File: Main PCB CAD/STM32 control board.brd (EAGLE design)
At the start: 120 x 100 mm, 193 parts, among them J10 B6B-PH, J15 DG301-4P, J16 B10B-PH, J17 B10B-PH, J18 B10B-PH, J19 B10B-PH, J20 B3B-PH, J21 B3B-PH, J22 B3B-PH, J23 B3B-PH, J4 PC_1733570, J5 PC_1733570, J6 B3B-PH, J7 B3B-PH, J8 B4B-PH, J9 B6B-PH, SW1 B3F-4055, SW2 B3F-4055, SW3 B3F-4055, SW4 B3F-4055, SW5 B3F-4055, U1 STM32G474, U2 TPS7A19, U3 REF3330, U4 REF3318, U5 ICM_20600, U6 DRV8701VIA, U8 L2293Q, X1 CSTNE

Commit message: Not finished consept
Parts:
- removed D2, D3, D4, D5: Blue, Semiconductor_devices:LED-0805
- removed RM1: RES_ARRAY0603, Resistors:0603-ARC
- moved J4 28.0 mm to (98.5, 117.0)
- moved J5 28.0 mm to (88.5, 117.0)
- moved RM5 18.8 mm to (105.4, 60.2), turned to 0 degrees
- moved RM3 18.0 mm to (82.4, 60.0), turned to 0 degrees
- moved J15 15.3 mm to (94.8, 89.8)
- moved D14 7.99 mm to (82.5, 46.2), turned to 0 degrees
- moved D15 7.99 mm to (82.5, 48.2), turned to 0 degrees
- moved D24 7.99 mm to (82.5, 50.2), turned to 0 degrees
- moved D25 7.99 mm to (82.5, 52.2), turned to 0 degrees
- moved D26 7.99 mm to (82.5, 54.2), turned to 0 degrees
- moved D35 7.99 mm to (82.5, 42.2), turned to 0 degrees
- moved D36 7.99 mm to (82.5, 44.2), turned to 0 degrees
- moved D37 7.99 mm to (82.5, 56.2), turned to 0 degrees
- moved J16 7.29 mm to (86.8, 49.2)
- moved RM2 5.70 mm to (82.4, 38.5)
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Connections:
- removed net N$13: D31.-, RM5.1
- removed net N$14: D32.-, RM5.2
- removed net N$17: D33.-, RM5.3
- removed net N$22: D34.-, RM5.4
- removed net PB1: D4.+, U1.33
- removed net PB2: D5.+, U1.34
- removed net PC6: D2.+, U1.65
- removed net PC7: D3.+, U1.66
- net GND: no longer RM1.5, RM1.6, RM1.7, RM1.8
- net N$10: now also D34.-, RM5.1; no longer D30.-, RM4.4
- net N$11: now also D28.-, RM4.3; no longer D5.-, RM1.4
- net N$12: now also RM4.4; no longer RM4.1
- net N$3: now also D30.-, RM4.1; no longer D28.-, RM4.2
- net N$4: now also D31.-, RM5.4; no longer D2.-, RM1.1
- net N$5: now also D32.-, RM5.3; no longer D3.-, RM1.2
- net N$6: now also D33.-, RM5.2; no longer D4.-, RM1.3
- net N$9: now also RM4.2; no longer RM4.3
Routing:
- net GND: track 59.2 -> 35.8 mm
- net PD0: track 64.4 -> 41.8 mm
- net N$22: track 20.8 -> 0.00 mm, vias 2 -> 0
- net PD1: track 63.5 -> 43.0 mm
- net PD2: track 63.1 -> 44.3 mm
- net N$17: track 18.4 -> 0.00 mm, vias 2 -> 0
- net PD3: track 62.1 -> 45.5 mm
- net N$14: track 16.1 -> 0.00 mm, vias 2 -> 0
- net N$31: track 20.8 -> 4.99 mm
- net PD4: track 62.3 -> 46.8 mm
- net PD5: track 62.5 -> 48.0 mm
- net N$13: track 13.8 -> 0.00 mm, vias 2 -> 0
- net PD6: track 62.8 -> 49.2 mm
- net PD8: track 29.6 -> 16.5 mm
- net PD7: track 63.0 -> 50.5 mm
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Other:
- outline, holes or cut-outs redrawn

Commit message: consept update
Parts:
- moved D27 3.29 mm to (108.8, 43.0), turned to 0 degrees
- moved D28 3.29 mm to (108.8, 45.0), turned to 0 degrees
- moved D29 3.29 mm to (108.8, 47.0), turned to 0 degrees
- moved D30 3.29 mm to (108.8, 49.0), turned to 0 degrees
- moved D31 3.29 mm to (108.8, 51.0), turned to 0 degrees
- moved D32 3.29 mm to (108.8, 53.0), turned to 0 degrees
- moved D33 3.29 mm to (108.8, 55.0), turned to 0 degrees
- moved D34 3.29 mm to (108.8, 57.0), turned to 0 degrees
- moved J19 3.29 mm to (113.0, 50.0)
- moved RM4 3.29 mm to (108.9, 39.3)
- moved RM5 3.29 mm to (108.6, 60.7)
- moved D14 0.75 mm to (82.5, 47.0)
- moved D15 0.75 mm to (82.5, 49.0)
- moved D24 0.75 mm to (82.5, 51.0)
- moved D25 0.75 mm to (82.5, 53.0)
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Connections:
- net N$10: now also D28.-, RM4.2; no longer D34.-, RM5.1
- net N$11: now also D29.-; no longer D28.-
- net N$12: now also D30.-; no longer D27.-
- net N$3: now also D34.-, RM5.4; no longer D30.-, RM4.1
- net N$4: now also D33.-, RM5.3; no longer D31.-, RM5.4
- net N$5: now also RM5.2; no longer RM5.3
- net N$6: now also D31.-, RM5.1; no longer D33.-, RM5.2
- net N$9: now also D27.-, RM4.1; no longer D29.-, RM4.2
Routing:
- net PD0: track 41.8 -> 69.2 mm
- net PD1: track 43.0 -> 68.6 mm
- net PD2: track 44.3 -> 68.1 mm
- net PD3: track 45.5 -> 67.5 mm
- net PD4: track 46.8 -> 67.0 mm
- net PD5: track 48.0 -> 66.4 mm
- net PD6: track 49.2 -> 65.9 mm
- net PD7: track 50.5 -> 65.3 mm
- net N$12: track 4.61 -> 12.1 mm
- net N$3: track 11.9 -> 4.96 mm
- net N$6: track 6.85 -> 12.2 mm
- net N$4: track 11.8 -> 7.29 mm
- net N$9: track 9.33 -> 4.87 mm
- net N$10: track 4.52 -> 7.20 mm
- net N$11: track 6.94 -> 9.60 mm
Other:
- outline, holes or cut-outs redrawn

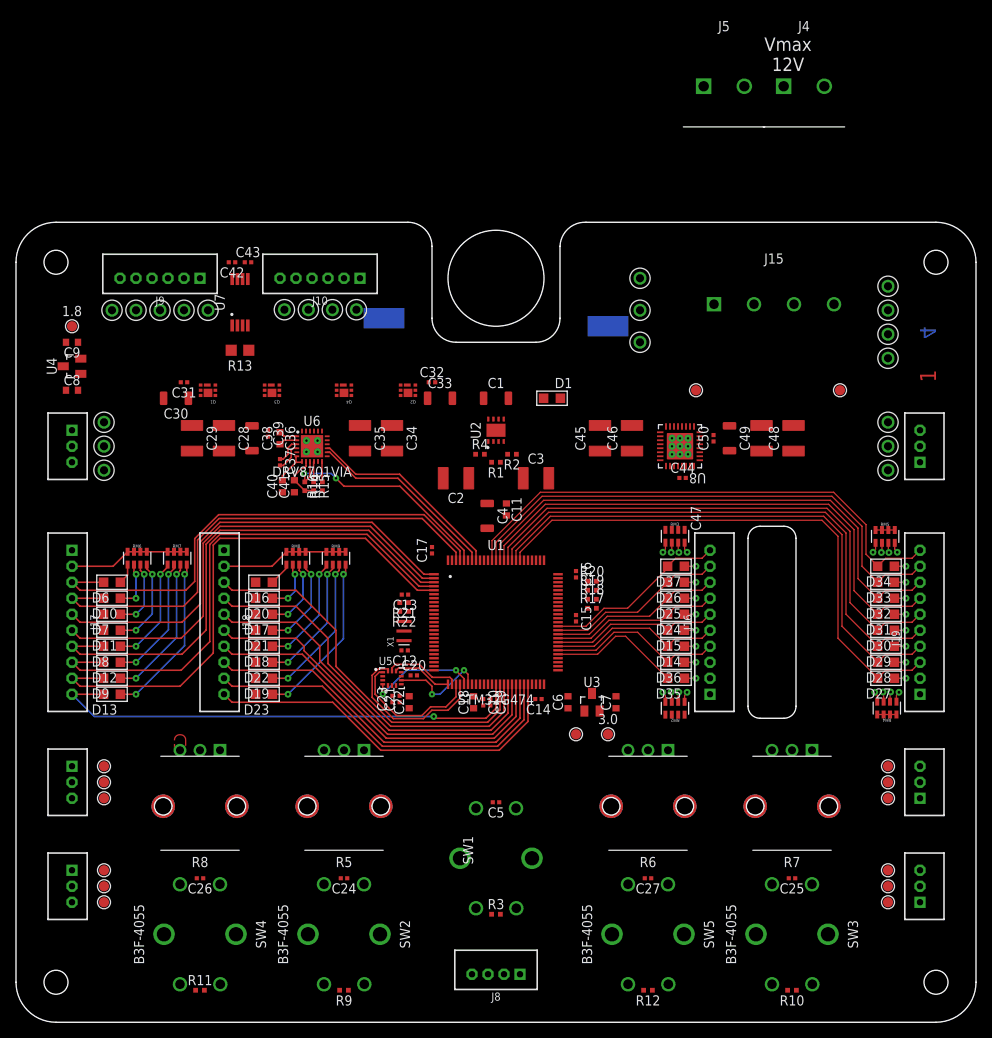
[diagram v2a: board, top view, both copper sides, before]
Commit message: placement fixes.
Current size is 104*120mm
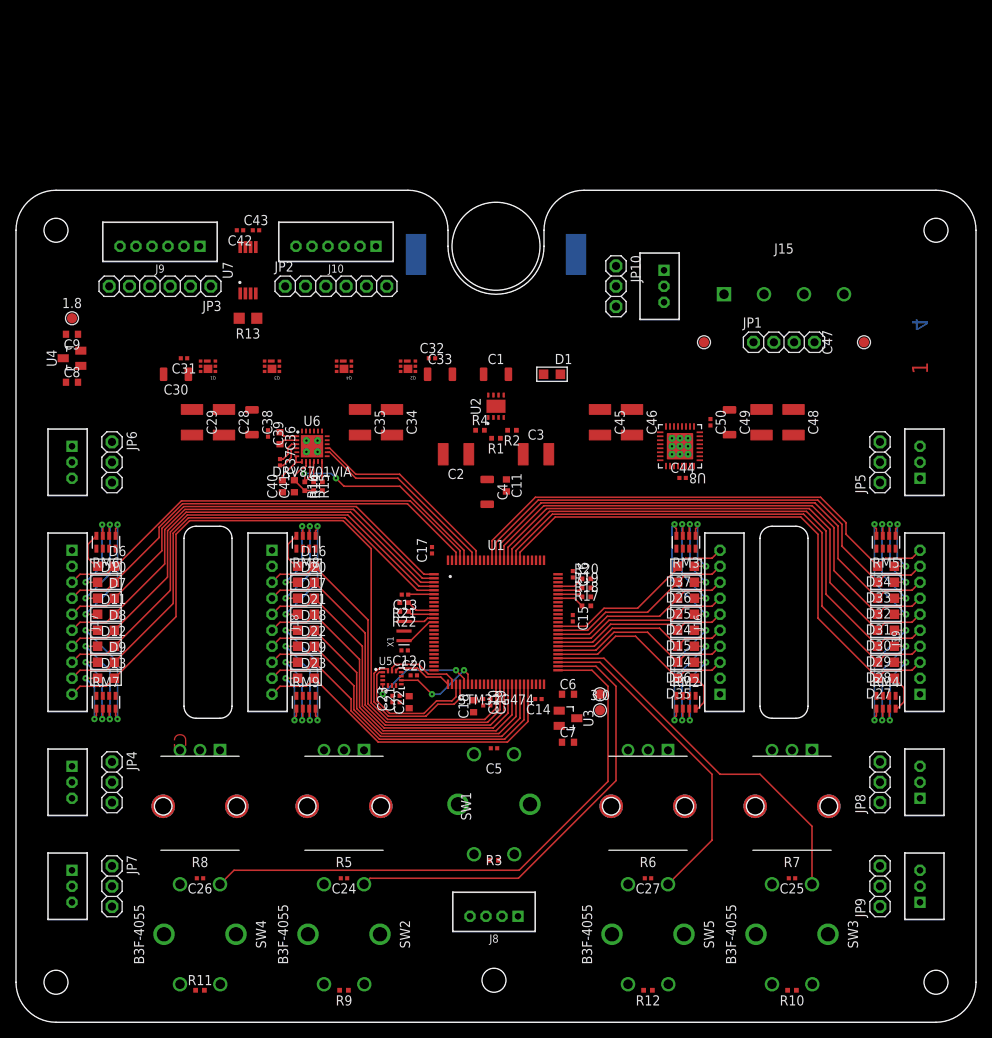
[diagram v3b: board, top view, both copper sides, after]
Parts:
- removed J4, J5: PC_1733570, Terminal blocks:PC_1733570
- removed TP1, TP18, TP19, TP2, TP20, TP21, TP22, TP23, TP24, TP25, TP26, TP27, TP28, TP29, TP3, TP30, TP31, TP32, TP33, TP34, TP35, TP36: (no value), testing:TEST_RING
- removed TP10, TP11, TP12, TP13, TP14, TP15, TP16, TP17, TP6, TP7, TP8, TP9: (no value), testing:TP1.27MM_MASK_SILKSCREEN
- added J1: B3B-PH, con-jst-ph:B3B-PH-K
- added JP1: (no value), commonly used connectors:1X04
- added JP10, JP4, JP5, JP6, JP7, JP8, JP9: (no value), commonly used connectors:1X03
- added JP2, JP3: (no value), commonly used connectors:1X06
- moved RM7 20.1 mm to (11.2, 40.0), turned to 180 degrees
- moved RM9 18.4 mm to (36.2, 40.0), turned to 180 degrees
- moved POS 9.85 mm to (70.0, 96.0), turned to 180 degrees
- moved NEG 8.94 mm to (50.0, 96.0), turned to 180 degrees
- moved C7 7.81 mm to (69.0, 35.0), turned to 0 degrees
- moved J8 7.25 mm to (59.8, 13.2)
- moved C5 6.75 mm to (59.8, 34.2)
- moved R3 6.75 mm to (59.8, 20.2)
- moved SW1 6.75 mm to (59.8, 27.2)
- moved TP38 6.71 mm to (106.0, 85.0)
- moved TP37 6.08 mm to (86.0, 85.0)
- moved J18 6.00 mm to (32.0, 50.0)
- moved GND_ 5.83 mm to (73.0, 41.0)
- moved D16 5.62 mm to (36.2, 57.0), turned to 180 degrees
- moved D17 5.62 mm to (36.2, 53.0), turned to 180 degrees
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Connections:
- removed net PC13: C26.1, R11.1, SW4.1, SW4.2, U1.7
- removed net PC14: C27.1, R12.1, SW5.1, SW5.2, U1.8
- new net PB12: C26.1, R11.1, SW4.1, SW4.2, U1.51
- new net PB13: C24.1, R9.1, SW2.1, SW2.2, U1.52
- net +3V: now also JP4.1, JP7.1, JP8.1, JP9.1; no longer TP12.1, TP15.1, TP6.1, TP9.1
- net +3V3: now also J1.2, JP10.2, JP2.2, JP3.1; no longer TP1.1
- net ENCODER_1: now also JP2.3; no longer TP30.1
- net ENCODER_2: now also JP2.4; no longer TP29.1
- net GND: now also J1.3, JP10.3, JP2.5, JP3.6, JP4.3, JP5.3, JP6.3, JP7.3, JP8.3, JP9.3, RM2.1, RM2.2, RM2.3, RM2.4, RM3.1, RM3.2, RM3.3, RM3.4, RM4.1, RM4.2, RM4.3, RM4.4, RM5.1, RM5.2, RM5.3, RM5.4, RM6.1, RM6.2, RM6.3, RM6.4, RM7.1, RM7.2, RM7.3, RM7.4, RM8.1, RM8.2, RM8.3, RM8.4, RM9.1, RM9.2, RM9.3, RM9.4; no longer RM2.5, RM2.6, RM2.7, RM2.8, RM3.5, RM3.6, RM3.7, RM3.8, RM4.5, RM4.6, RM4.7, RM4.8, RM5.5, RM5.6, RM5.7, RM5.8, RM6.5, RM6.6, RM6.7, RM6.8, RM7.5, RM7.6, RM7.7, RM7.8, RM8.5, RM8.6, RM8.7, RM8.8, RM9.5, RM9.6, RM9.7, RM9.8, TP11.1, TP14.1, TP17.1, TP20.1, TP21.1, TP26.1, TP3.1, TP32.1, TP8.1
- net I2C3_SCL: now also JP5.2; no longer TP27.1
- net I2C3_SDA: now also JP5.1; no longer TP28.1
- net M1: now also JP2.1; no longer TP31.1
- net M_SH2: now also JP2.6
- net N$10: now also RM4.7; no longer RM4.2
- net N$11: now also RM4.6; no longer RM4.3
- net N$12: now also RM4.5; no longer RM4.4
- net N$23: now also RM2.8; no longer RM2.1
- net N$25: now also RM2.7; no longer RM2.2
- net N$26: now also RM2.6; no longer RM2.3
- net N$27: now also RM2.5; no longer RM2.4
- net N$28: now also RM3.8; no longer RM3.1
- net N$29: now also RM3.7; no longer RM3.2
- net N$3: now also RM5.5; no longer RM5.4
- net N$30: now also RM3.6; no longer RM3.3
- net N$31: now also RM3.5; no longer RM3.4
- net N$34: now also RM6.8; no longer RM6.1
- net N$35: now also RM6.7; no longer RM6.2
- net N$36: now also RM6.6; no longer RM6.3
- net N$38: now also RM6.5; no longer RM6.4
- net N$39: now also RM7.8; no longer RM7.1
- net N$4: now also RM5.6; no longer RM5.3
- net N$40: now also RM7.7; no longer RM7.2
- net N$41: now also RM7.6; no longer RM7.3
- net N$42: now also RM7.5; no longer RM7.4
- net N$43: now also RM8.8; no longer RM8.1
- net N$44: now also RM8.7; no longer RM8.2
- net N$45: now also RM8.6; no longer RM8.3
- net N$46: now also RM8.5; no longer RM8.4
- net N$47: now also RM9.8; no longer RM9.1
- net N$48: now also RM9.7; no longer RM9.2
- net N$49: now also RM9.6; no longer RM9.3
- net N$5: now also RM5.7; no longer RM5.2
- net N$50: now also RM9.5; no longer RM9.4
- net N$6: now also RM5.8; no longer RM5.1
- net N$9: now also RM4.8; no longer RM4.1
- net PA0: now also JP9.2; no longer TP7.1
- net PA1: now also JP8.2; no longer TP10.1
- net PA2: now also JP7.2; no longer TP13.1
- net PA3: now also JP4.2; no longer TP16.1
- net PB14: now also C27.1, R12.1, SW5.1, SW5.2; no longer C24.1, R9.1, SW2.1, SW2.2
- net PO1: now also JP1.1; no longer J5.2, TP33.1
- net PO2: now also JP1.2; no longer J5.1, TP34.1
- net PO3: now also JP1.3; no longer J4.2, TP35.1
- net PO4: now also JP1.4; no longer J4.1, TP36.1
- net SPI3_MISO: now also JP3.3; no longer TP24.1
- net SPI3_MOSI: now also JP3.2; no longer TP25.1
- net SPI3_SCK: now also JP3.4; no longer TP23.1
- net SPI_CS: now also JP3.5; no longer TP22.1
- net USART3_RX: now also JP6.2; no longer TP19.1
- net USART3_TX: now also JP6.1; no longer TP18.1
- net VDD: now also J1.1, JP10.1; no longer TP2.1
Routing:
- net PB12: track 0.00 -> 72.8 mm
- net PB13: track 0.00 -> 56.9 mm
- net PB15: track 0.00 -> 47.7 mm
- net PB14: track 0.00 -> 41.1 mm
- net GND: track 35.8 -> 0.00 mm
- net PE7: track 61.7 -> 93.2 mm, vias 1 -> 0
- net N$50: track 21.1 -> 8.76 mm
- net N$42: track 20.8 -> 8.46 mm
- net N$49: track 18.8 -> 11.1 mm
- net N$41: track 18.5 -> 10.8 mm
- net PD8: track 16.8 -> 24.2 mm
- net PE0: track 63.0 -> 56.5 mm
- net PE1: track 63.5 -> 57.2 mm
- net PE4: track 65.0 -> 59.2 mm
- net PE5: track 66.5 -> 60.8 mm
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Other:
- board size 120 x 100 mm -> 120 x 104 mm
- board text removed: "Vmax 12V"

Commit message: routing
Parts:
- removed JP10: (no value), commonly used connectors:1X03
- moved J20 106.8 mm to (7.00, 30.0), turned to 270 degrees
- moved J21 106.8 mm to (7.00, 17.0), turned to 270 degrees
- moved J22 106.8 mm to (113.0, 30.0), turned to 90 degrees
- moved J23 106.8 mm to (113.0, 17.0), turned to 90 degrees
- moved J6 106.0 mm to (7.00, 70.0), turned to 270 degrees
- moved J7 106.0 mm to (113.0, 70.0), turned to 90 degrees
- moved JP4 96.9 mm to (108.0, 17.0), turned to 90 degrees
- moved JP7 96.9 mm to (108.0, 30.0), turned to 90 degrees
- moved JP8 96.9 mm to (12.0, 17.0), turned to 270 degrees
- moved JP9 96.9 mm to (12.0, 30.0), turned to 270 degrees
- moved JP5 96.0 mm to (12.0, 70.0), turned to 270 degrees
- moved JP6 96.0 mm to (108.0, 70.0), turned to 90 degrees
- moved R8 74.0 mm to (97.0, 34.0)
- moved R6 38.0 mm to (41.0, 34.0)
- moved R21 30.2 mm to (78.0, 59.0), turned to 90 degrees
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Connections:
- removed net M1: J10.1, JP2.1, R13.2, U7.2
- new net M2: J10.6, JP2.6, R13.2, U7.3
- net +3V3: no longer JP10.2
- net BRIDGE1_EN: now also U1.65; no longer U1.10
- net BRIDGE2_EN: now also U1.66; no longer U1.11
- net GND: no longer JP10.3
- net M_SH1: now also J10.1, JP2.1; no longer R13.1, U7.3
- net M_SH2: now also R13.1, U7.2; no longer J10.6, JP2.6
- net PO2: now also J15.3; no longer J15.1
- net PO4: now also J15.1; no longer J15.3
- net VDD: no longer JP10.1
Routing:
- net SPI_CS: track 0.00 -> 81.0 mm, vias 0 -> 1
- net SPI3_SCK: track 0.00 -> 79.7 mm, vias 0 -> 1
- net SPI3_MISO: track 0.00 -> 78.7 mm, vias 0 -> 1
- net SPI3_MOSI: track 0.00 -> 77.9 mm, vias 0 -> 1
- net PA3: track 0.00 -> 70.0 mm, vias 0 -> 1
- net I2C3_SDA: track 0.00 -> 69.9 mm, vias 0 -> 1
- net I2C3_SCL: track 0.00 -> 69.0 mm, vias 0 -> 1
- net PA2: track 0.00 -> 64.7 mm, vias 0 -> 1
- net USART3_RX: track 0.00 -> 59.4 mm, vias 0 -> 1
- net USART3_TX: track 0.00 -> 57.7 mm, vias 0 -> 1
- net PC3: track 0.00 -> 55.6 mm, vias 0 -> 1
- net PA1: track 0.00 -> 55.3 mm, vias 0 -> 1
- net PA0: track 0.00 -> 48.9 mm, vias 0 -> 1
- net SWDIO: track 0.00 -> 47.7 mm, vias 0 -> 1
- net SWCLK: track 0.00 -> 47.7 mm, vias 0 -> 1
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- added copper zone on layer 1, net +3V3
- added copper zone on layer 1, net AVDD1
- added copper zone on layer 2, net GND
- added copper zone on layer 1, net M2
- added copper zone on layer 1, net M_SH1
- added copper zone on layer 1, net M_SH2
- added copper zone on layer 1, net VDD
- added copper zone on layer 15, net VDD

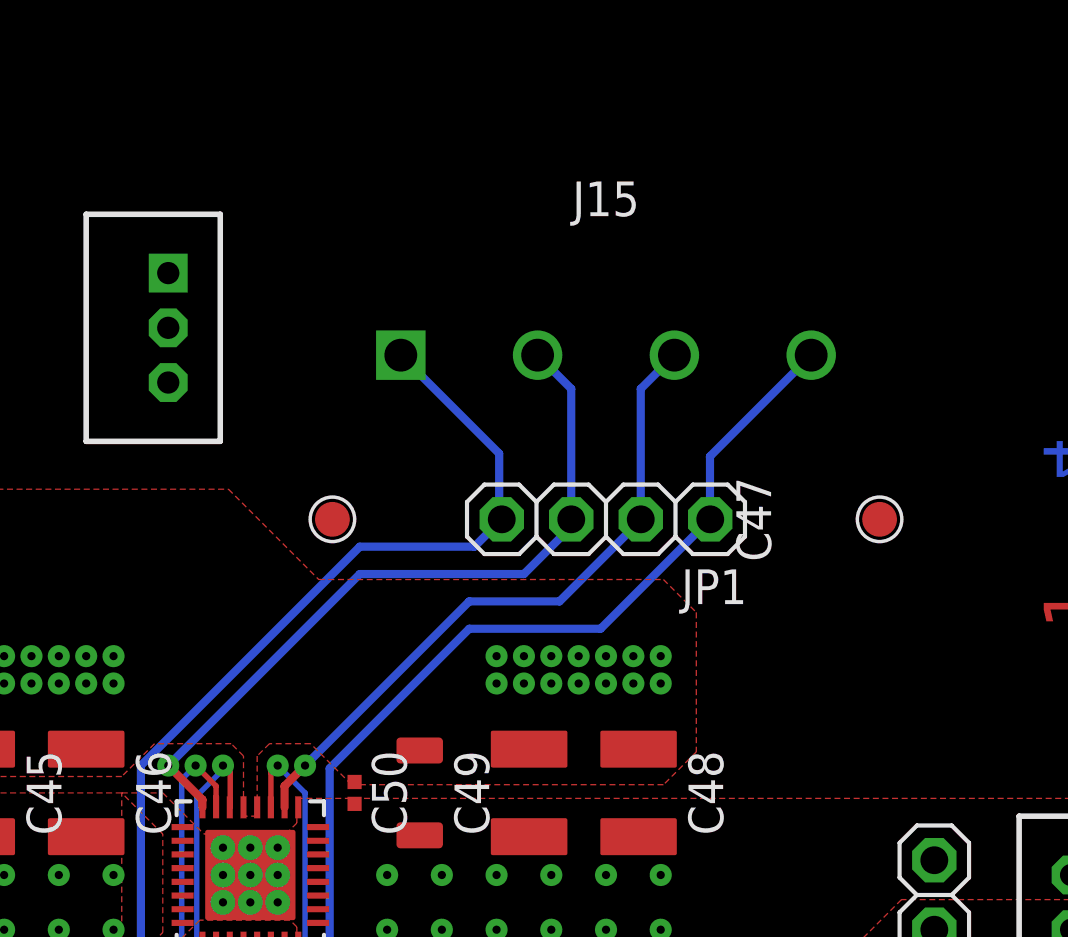
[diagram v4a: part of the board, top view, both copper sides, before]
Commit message: screw terminal placement fix
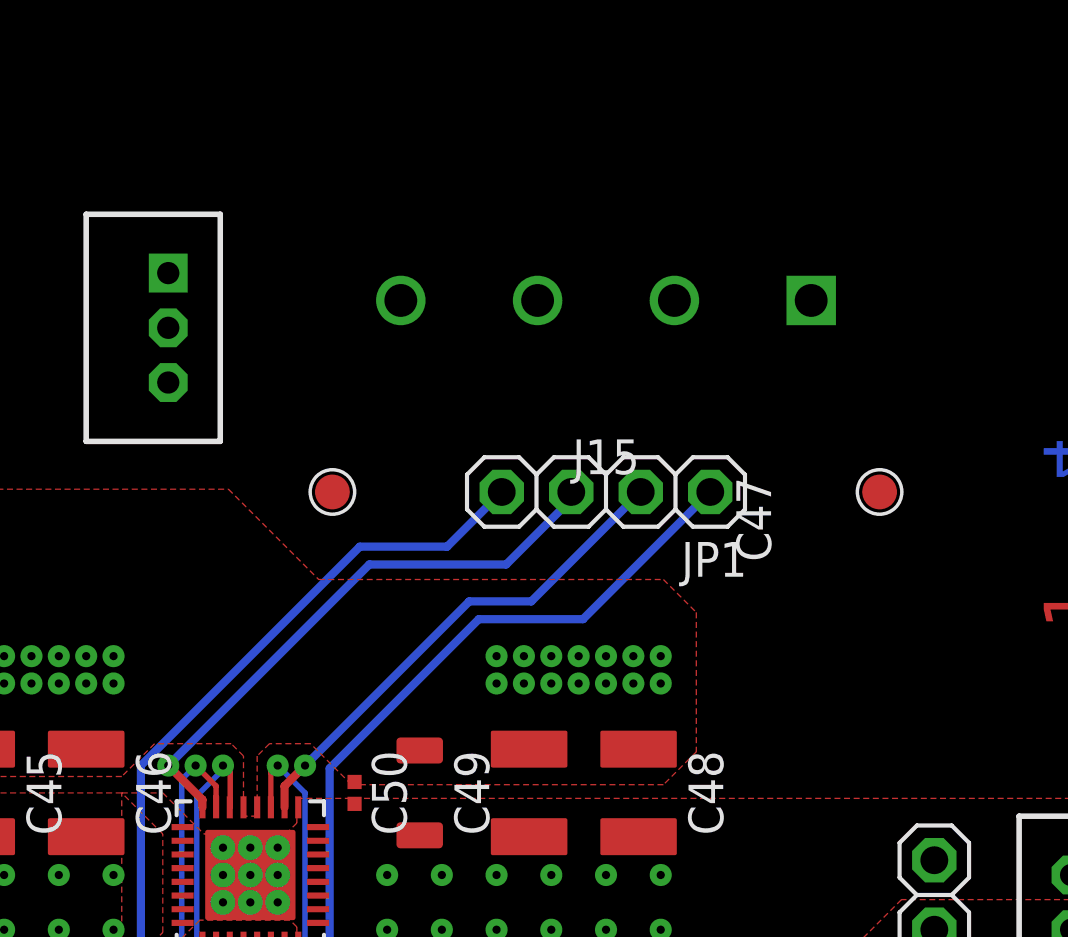
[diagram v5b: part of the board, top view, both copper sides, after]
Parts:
- moved J15 2.00 mm to (96.0, 93.0), turned to 180 degrees
- moved JP1 1.00 mm to (96.0, 86.0)
- moved TP37 1.00 mm to (86.0, 86.0)
- moved TP38 1.00 mm to (106.0, 86.0)
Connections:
- net PO1: now also J15.1; no longer J15.4
- net PO2: now also J15.2; no longer J15.3
- net PO3: now also J15.3; no longer J15.2
- net PO4: now also J15.4; no longer J15.1
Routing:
- net PO4: track 35.0 -> 27.8 mm
- net PO1: track 35.7 -> 28.6 mm
- net PO2: track 24.4 -> 18.2 mm
- net PO3: track 27.2 -> 21.1 mm

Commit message: routing part 2
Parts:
- added TP1, TP2, TP3: 1.8, testing:TP1.27MM_MASK_SILKSCREEN
- moved TP4 43.1 mm to (113.0, 23.0)
- moved GND_ 39.4 mm to (108.0, 23.0)
- moved TP37 20.0 mm to (106.0, 86.0)
- moved TP38 20.0 mm to (86.0, 86.0)
- moved C5 9.90 mm to (67.0, 27.0), turned to 90 degrees
- moved R3 9.90 mm to (53.0, 27.0), turned to 270 degrees
- moved TP5 2.00 mm to (7.00, 78.0)
- moved J1 1.50 mm to (78.5, 92.0), turned to 90 degrees
- moved C13 0.50 mm to (49.6, 53.0)
- moved C10 0.25 mm to (58.2, 39.9)
- moved C19 0.25 mm to (59.1, 39.9)
- moved C18 0.20 mm to (57.0, 39.5)
- turned C8 to 0 degrees
- turned R11 to 180 degrees
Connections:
- net +3V3: now also TP2.1
- net GND: now also TP1.1, TP3.1
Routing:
- net +3V3: track 20.4 -> 684.8 mm, vias 10 -> 23
- net +3V: track 0.00 -> 172.1 mm, vias 0 -> 3
- net MOTOR_CS: track 0.00 -> 72.0 mm, vias 0 -> 2
- net GND: track 47.6 -> 107.5 mm, vias 101 -> 217
- net N$20: track 28.2 -> 76.9 mm, vias 2 -> 3
- net +1.8V: track 0.00 -> 47.9 mm, vias 0 -> 2
- net N$19: track 13.4 -> 47.9 mm, vias 2 -> 3
- net RST: track 21.4 -> 52.8 mm
- net PB14: track 41.1 -> 59.5 mm
- net PB15: track 47.7 -> 66.2 mm
- net PB13: track 56.9 -> 75.4 mm
- net PB12: track 72.8 -> 91.3 mm
- net PO4: track 27.8 -> 36.3 mm
- net PO1: track 28.6 -> 37.1 mm
- net PO3: track 21.1 -> 28.6 mm
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- added copper zone on layer 1, net +1.8V
- added copper zone on layer 16, net GND
- added copper zone on layer 16, net VDD

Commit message: routing part 3
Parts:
- R5, R6, R7, R8: device Resistors:ALPS_PTM -> Resistors:ALPS_PTM_LONG
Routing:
- net +3V3: track 684.8 -> 686.6 mm
- net +3V: track 172.1 -> 173.7 mm
- net PA3: track 75.0 -> 75.6 mm
- net PA2: track 69.7 -> 70.3 mm
- net PC3: track 55.6 -> 56.1 mm
- net GND: vias 217 -> 244

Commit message: polygons part 1
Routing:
- net +3V3: track 686.6 -> 693.9 mm
- added copper zone on layer 1, net +3V
- added copper zone on layer 15, net +3V
- added copper zone on layer 15, net +3V3
- added copper zone on layer 15, net GND
